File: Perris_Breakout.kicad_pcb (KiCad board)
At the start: 2 copper layers, 67.3 x 67.3 mm, 21 parts, among them J1 PERRI_1, J10 SDA, J11 GND, J12 GND, J13 SCL, J14 SCL, J2 PERRI_2, J3 PERRI_3, J4 PERRI_4, J5 PERRI_5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

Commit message: More Perris
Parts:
- removed TP1: SDA, TestPoint:TestPoint_Pad_2.5x2.5mm
- removed TP2: GND, TestPoint:TestPoint_Pad_2.5x2.5mm
- removed TP3: SCL, TestPoint:TestPoint_Pad_2.5x2.5mm
- added J15: PERRI_15, HELIX:Perri_conn_2x5_Reverse, F.Cu at (140.2, 86.4)
- added J16: PERRI_16, HELIX:Perri_conn_2x5_Reverse, F.Cu at (152.4, 86.4)
- added J17: PERRI_17, HELIX:Perri_conn_2x5_Reverse, F.Cu at (22.0, 138.4)
- added J18: PERRI_18, HELIX:Perri_conn_2x5_Reverse, F.Cu at (34.1, 138.4)
- added J19: PERRI_19, HELIX:Perri_conn_2x5_Reverse, F.Cu at (22.0, 157.9)
- added J20: PERRI_20, HELIX:Perri_conn_2x5_Reverse, F.Cu at (34.1, 157.9)
- added J21: PERRI_21, HELIX:Perri_conn_2x5_Reverse, F.Cu at (140.3, 138.4)
- added J22: PERRI_22, HELIX:Perri_conn_2x5_Reverse, F.Cu at (152.4, 138.4)
- added J23: PERRI_23, HELIX:Perri_conn_2x5_Reverse, F.Cu at (140.3, 157.9)
- added J24: PERRI_24, HELIX:Perri_conn_2x5_Reverse, F.Cu at (152.4, 157.9)
- added J25: Probe 0, Connector_PinHeader_2.54mm:PinHeader_1x03_P2.54mm_Vertical, F.Cu at (73.0, 116.5)
- added J26: Probe 1, Connector_PinHeader_2.54mm:PinHeader_1x03_P2.54mm_Vertical, F.Cu at (86.0, 116.9)
- added J27: Probe 2, Connector_PinHeader_2.54mm:PinHeader_1x03_P2.54mm_Vertical, F.Cu at (110.4, 117.4)
- added J28: Probe 3, Connector_PinHeader_2.54mm:PinHeader_1x03_P2.54mm_Vertical, F.Cu at (105.8, 117.4)
- added J29: Power, Connector_Molex:Molex_Micro-Fit_3.0_43650-0400_1x04_P3.00mm_Horizontal, F.Cu at (82.0, 185.0)
- added R1: Resistor, Resistor_SMD:R_0805_2012Metric, F.Cu at (89.8, 145.5)
- added R2: Resistor, Resistor_SMD:R_0805_2012Metric, F.Cu at (81.0, 145.5)
- added R3: Resistor, Resistor_SMD:R_0805_2012Metric, F.Cu at (81.0, 148.4)
- added R4: Resistor, Resistor_SMD:R_0805_2012Metric, F.Cu at (98.6, 148.3)
- added R5: Resistor, Resistor_SMD:R_0805_2012Metric, F.Cu at (85.4, 148.4)
- added R6: Resistor, Resistor_SMD:R_0805_2012Metric, F.Cu at (85.4, 145.5)
- added R7: Resistor, Resistor_SMD:R_0805_2012Metric, F.Cu at (94.2, 148.3)
- added R8: Resistor, Resistor_SMD:R_0805_2012Metric, F.Cu at (89.8, 148.4)
- added U1: EK-TM4C123GXL, HELIX:TM4C123GXL_launchpad_male_connector, F.Cu at (86.5, 53.2)
- H1, H2, H3, H4: value MountingHole_Pad -> Mount
- J10: value SDA -> PERRI_10; footprint Connector_PinHeader_2.54mm:PinHeader_1x01_P2.54mm_Vertical -> HELIX:Perri_conn_2x5_Reverse
- J11: value GND -> PERRI_11; footprint Connector_PinHeader_2.54mm:PinHeader_1x01_P2.54mm_Vertical -> HELIX:Perri_conn_2x5_Reverse
- J12: value GND -> PERRI_12; footprint Connector_PinHeader_2.54mm:PinHeader_1x01_P2.54mm_Vertical -> HELIX:Perri_conn_2x5_Reverse
- J13: value SCL -> PERRI_13; footprint Connector_PinHeader_2.54mm:PinHeader_1x01_P2.54mm_Vertical -> HELIX:Perri_conn_2x5_Reverse
- J14: value SCL -> PERRI_14; footprint Connector_PinHeader_2.54mm:PinHeader_1x01_P2.54mm_Vertical -> HELIX:Perri_conn_2x5_Reverse
- J9: value SDA -> PERRI_9; footprint Connector_PinHeader_2.54mm:PinHeader_1x01_P2.54mm_Vertical -> HELIX:Perri_conn_2x5_Reverse
- moved H3 165.0 mm to (6.35, 184.2)
- moved H1 144.5 mm to (6.35, 19.1)
- moved J5 118.1 mm to (22.0, 67.0), turned to 0 degrees
- moved H2 112.5 mm to (171.4, 19.1)
- moved J6 107.5 mm to (34.1, 67.0), turned to 0 degrees
- moved J8 105.6 mm to (34.1, 86.5), turned to 0 degrees
- moved J7 100.9 mm to (22.0, 86.5), turned to 0 degrees
- moved J4 99.6 mm to (34.3, 47.1), turned to 0 degrees
- moved J3 95.3 mm to (22.0, 47.1), turned to 0 degrees
- moved H4 88.0 mm to (171.4, 184.2)
- moved J1 84.1 mm to (22.0, 27.5)
- moved J2 81.4 mm to (34.3, 27.5)
- moved J9 45.8 mm to (140.2, 27.4)
- moved J10 43.0 mm to (152.5, 27.4)
- moved J11 37.9 mm to (140.2, 47.0)
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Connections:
- H1 pad 1: /GND -> GND
- H2 pad 1: /GND -> GND
- H3 pad 1: /GND -> GND
- H4 pad 1: /GND -> GND
- J1 pad 10: /GND -> GND
- J1 pad 5: /SCL -> /SCL_0
- J1 pad 6: /SDA -> /SDA_0
- J10 pad 1: /SDA -> unconnected-(J10-Pad1)
- J11 pad 1: /GND -> unconnected-(J11-Pad1)
- J12 pad 1: /GND -> unconnected-(J12-Pad1)
- J13 pad 1: /SCL -> unconnected-(J13-Pad1)
- J14 pad 1: /SCL -> unconnected-(J14-Pad1)
- J2 pad 10: /GND -> GND
- J2 pad 5: /SCL -> /SCL_0
- J2 pad 6: /SDA -> /SDA_0
- J3 pad 10: /GND -> GND
- J3 pad 5: /SCL -> /SCL_0
- J3 pad 6: /SDA -> /SDA_0
- J4 pad 10: /GND -> GND
- J4 pad 5: /SCL -> /SCL_0
- J4 pad 6: /SDA -> /SDA_0
- J5 pad 10: /GND -> GND
- J5 pad 5: /SCL -> /SCL_0
- J5 pad 6: /SDA -> /SDA_0
- J6 pad 10: /GND -> GND
- J6 pad 5: /SCL -> /SCL_0
- J6 pad 6: /SDA -> /SDA_0
- J7 pad 10: /GND -> GND
- J7 pad 5: /SCL -> /SCL_0
- J7 pad 6: /SDA -> /SDA_0
- J8 pad 10: /GND -> GND
- J8 pad 5: /SCL -> /SCL_0
- J8 pad 6: /SDA -> /SDA_0
- J9 pad 1: /SDA -> unconnected-(J9-Pad1)
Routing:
- net /SDA_0: track 0.00 -> 257.2 mm
- net /SDA: track 213.1 -> 0.00 mm
- net /SCL_0: track 0.00 -> 184.4 mm
- net /SCL_1: track 0.00 -> 160.2 mm
- net /SCL: track 152.0 -> 0.00 mm
- net /SDA_1: track 0.00 -> 146.4 mm
- net /GND: track 17.1 -> 0.00 mm
- added copper zone on B.Cu, net GND
- removed copper zone on F.Cu, net /GND
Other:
- board size 67.3 x 67.3 mm -> 177.8 x 177.8 mm

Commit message: Finished placin compononets onto PCB.
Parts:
- moved R1 28.0 mm to (67.7, 128.4), turned to -90 degrees
- moved R8 27.1 mm to (108.2, 128.5), turned to -90 degrees
- moved R4 25.5 mm to (82.7, 128.5), turned to -90 degrees
- moved R7 22.9 mm to (105.7, 128.5), turned to -90 degrees
- moved R5 21.5 mm to (93.2, 128.4), turned to -90 degrees
- moved R2 20.1 mm to (70.2, 128.5), turned to -90 degrees
- moved R3 20.0 mm to (80.2, 128.5), turned to -90 degrees
- moved R6 19.9 mm to (95.7, 128.5), turned to -90 degrees
- moved J27 15.4 mm to (95.7, 122.0), turned to -90 degrees
- moved J25 6.21 mm to (70.2, 122.0), turned to -90 degrees
- moved J26 6.05 mm to (82.7, 122.0), turned to -90 degrees
- moved J28 5.20 mm to (108.2, 122.0), turned to -90 degrees
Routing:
- net /SDA_2: track 0.00 -> 212.1 mm
- net /SCL_2: track 0.00 -> 197.3 mm
- net /SCL_3: track 0.00 -> 107.9 mm
- net /SDA_3: track 0.00 -> 85.9 mm
- net +5V: track 0.00 -> 10.0 mm
- net /SDA_1: track 146.4 -> 154.8 mm
- net /SDA_0: track 257.2 -> 262.2 mm
- net /SCL_1: track 160.2 -> 165.2 mm
- net /SCL_0: track 184.4 -> 189.4 mm

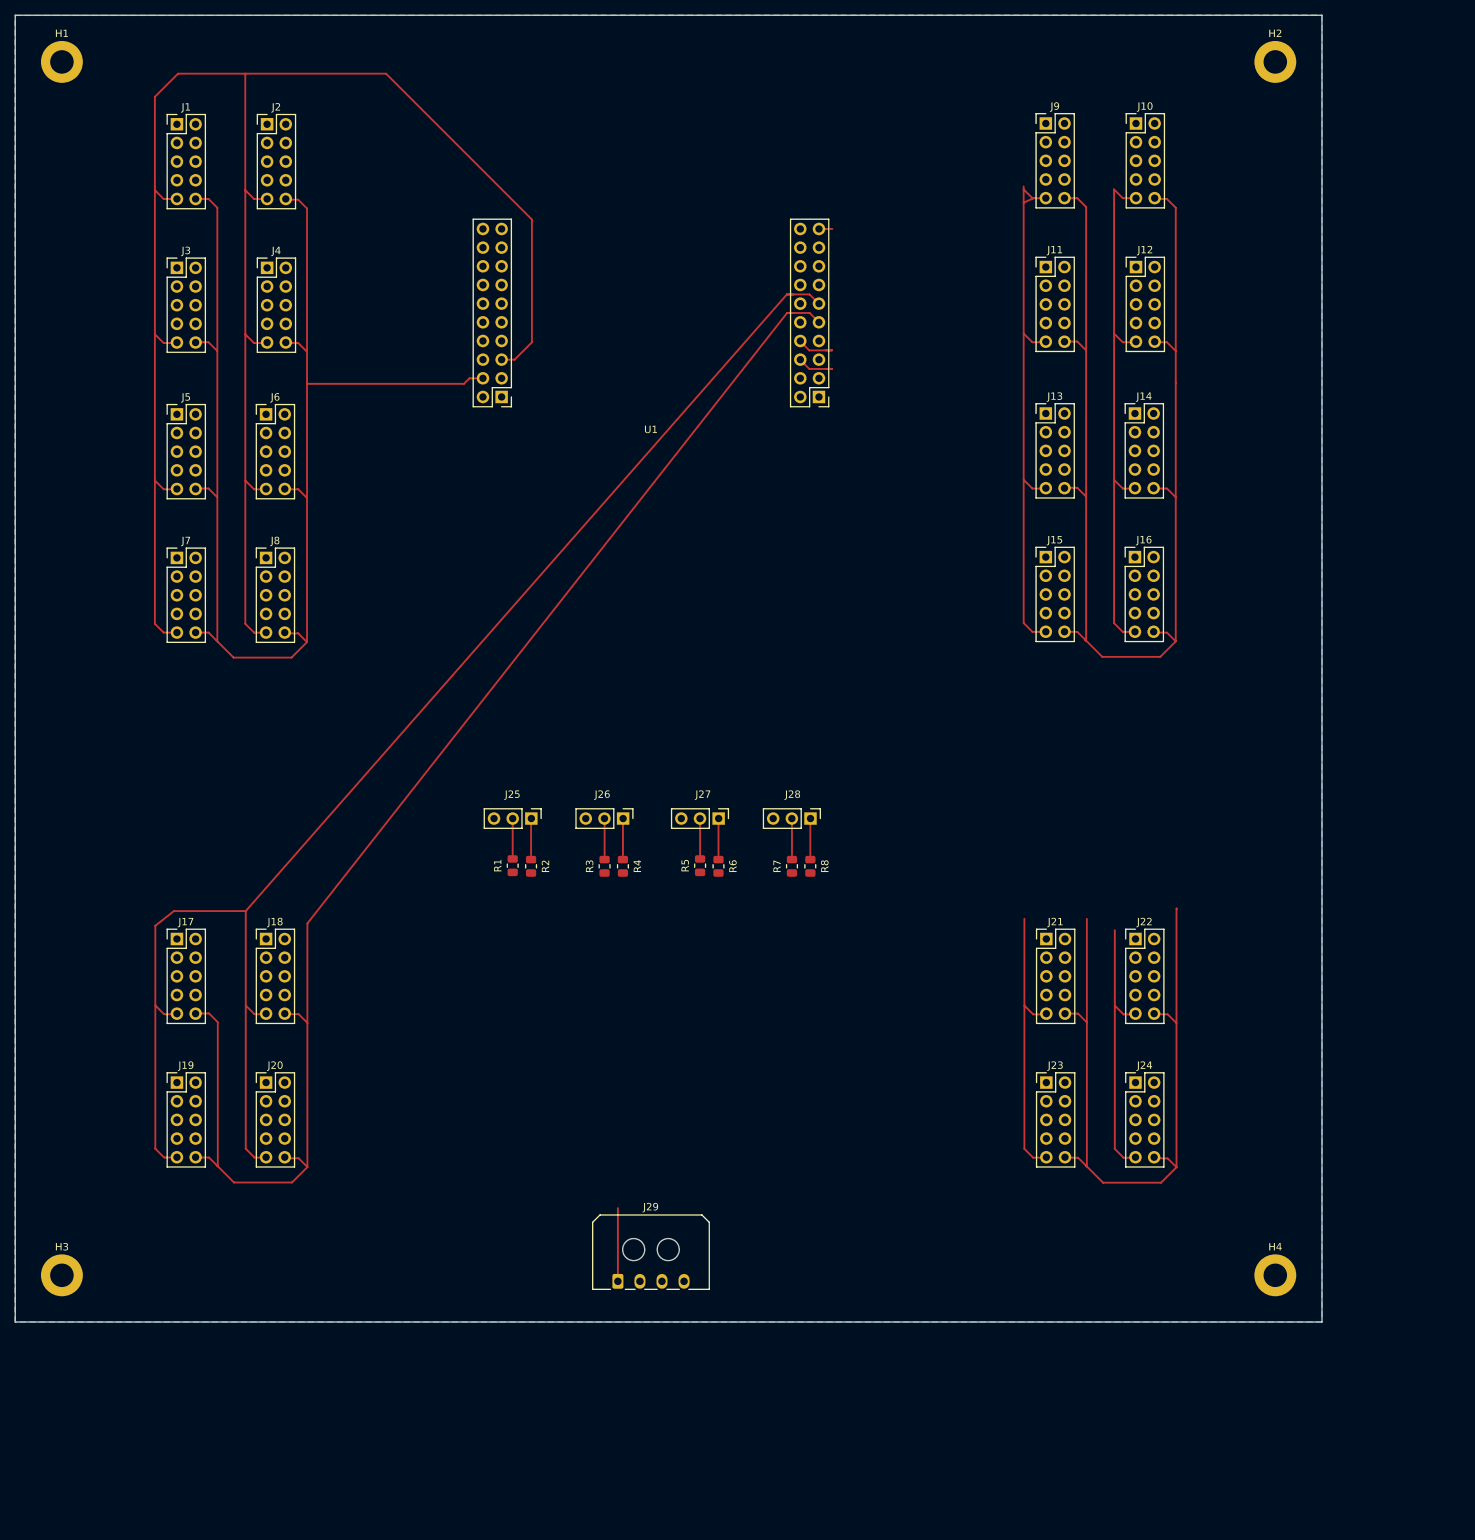
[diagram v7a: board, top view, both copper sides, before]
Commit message: Updated silk screens and rearranged components.
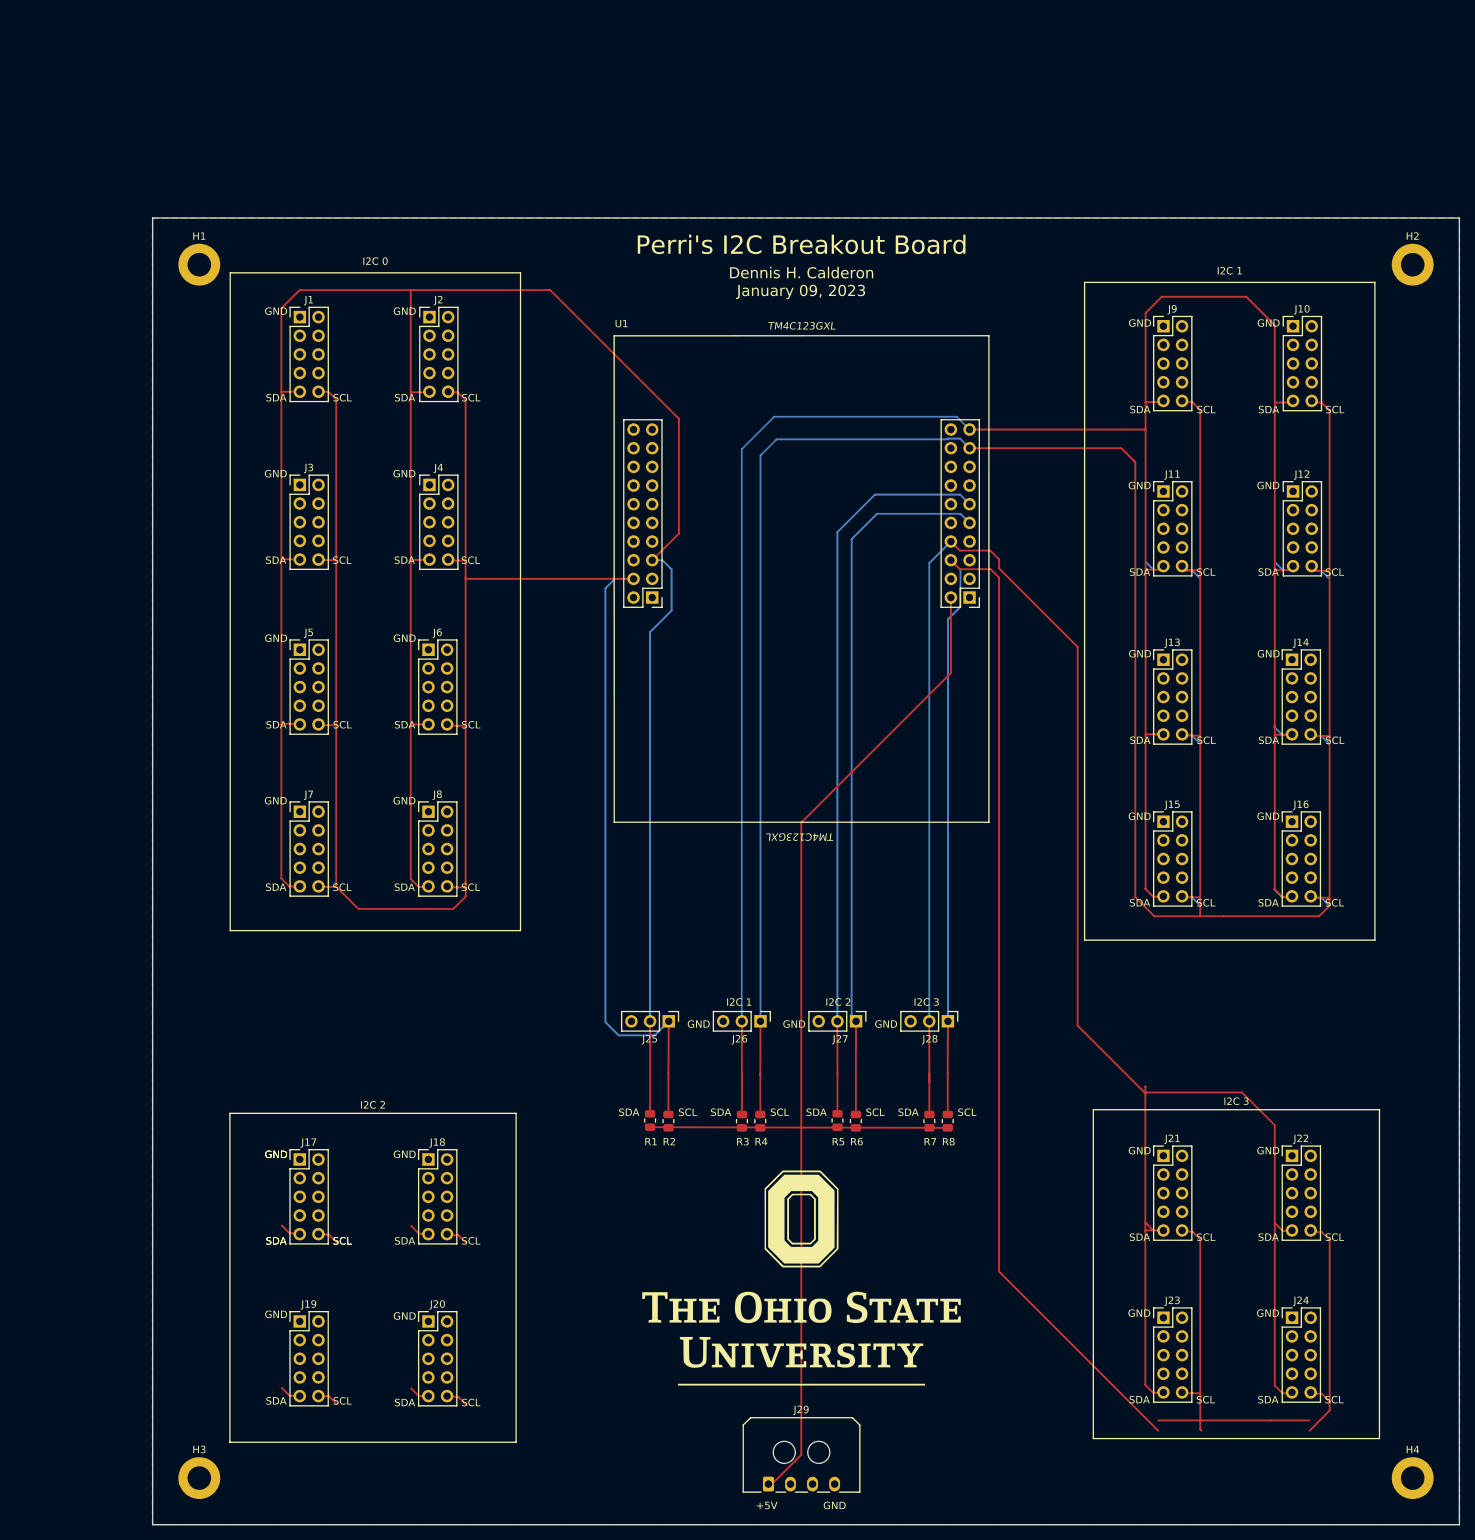
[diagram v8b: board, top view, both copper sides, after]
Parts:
- added G***: LOGO, LOGO, F.Cu at (107.0, 184.5)
- moved J16 41.9 mm to (173.7, 122.4)
- moved J8 41.0 mm to (56.2, 121.1)
- moved J14 39.7 mm to (173.7, 100.4)
- moved J15 39.4 mm to (156.2, 122.4)
- moved R1 39.4 mm to (86.4, 163.1)
- moved R2 39.4 mm to (88.9, 163.2)
- moved R3 39.4 mm to (98.9, 163.2)
- moved R4 39.4 mm to (101.4, 163.2)
- moved R5 39.4 mm to (111.9, 163.1)
- moved R6 39.4 mm to (114.4, 163.2)
- moved R7 39.4 mm to (124.4, 163.2)
- moved R8 39.4 mm to (126.9, 163.2)
- moved J20 39.3 mm to (56.2, 190.4)
- moved J6 38.9 mm to (56.2, 99.0)
- moved J24 38.4 mm to (173.7, 189.9)
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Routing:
- net /SCL_1: track 165.2 -> 404.5 mm
- net /SDA_1: track 154.8 -> 357.2 mm
- net /SDA_3: track 85.9 -> 276.7 mm
- net /SCL_3: track 107.9 -> 294.3 mm
- net +5V: track 10.0 -> 171.7 mm
- net /SDA_2: track 212.1 -> 111.0 mm
- net /SCL_0: track 189.4 -> 283.0 mm
- net /SCL_2: track 197.3 -> 107.6 mm
- net /SDA_0: track 262.2 -> 340.0 mm
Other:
- board text added: "+5V"
- board text added: "Dennis H. Calderon January 09, 2023"
- board text added: "GND"
- board text added: "I2C 0"
- board text added: "I2C 1"
- board text added: "I2C 2"
- board text added: "I2C 3"
- board text added: "Perri's I2C Breakout Board"
- board text added: "SCL"
- board text added: "SDA"
- board text added: "TM4C123GXL"
